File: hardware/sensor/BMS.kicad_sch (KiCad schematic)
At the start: 1 part, among them J4 Conn_01x04

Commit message: Fix incorrect upstream
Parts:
- removed J4: Conn_01x04, symbol Connector_Generic:Conn_01x04
- added J201: PWR, Connector_PinHeader_2.54mm:PinHeader_1x04_P2.54mm_Horizontal, symbol Connector:Conn_01x04_Pin
- added J202: control signals, Connector_PinHeader_2.54mm:PinHeader_1x06_P2.54mm_Horizontal, symbol Connector:Conn_01x06_Pin
- added J502: V_{DD}MCU, testpoint_519x:Testpoint_519xTR, symbol Connector:Conn_01x01_Pin
- added J502 (x3): GND, testpoint_519x:Testpoint_519xTR, symbol Connector:Conn_01x01_Pin
- added J502: V_{DD}AN, testpoint_519x:Testpoint_519xTR, symbol Connector:Conn_01x01_Pin
- added J502: LDO_{EN}, testpoint_519x:Testpoint_519xTR, symbol Connector:Conn_01x01_Pin
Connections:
- net GND: now also J201.2 (Pin_2), J201.3 (Pin_3), J202.5 (Pin_5), J502.1 (Pin_1), J502.1 (Pin_1), J502.1 (Pin_1)
- net V_{Out}: now also J201.4 (Pin_4), J502.1 (Pin_1)
- new net EH-ON: J202.3 (Pin_3)
- new net HBO-MCU: J202.4 (Pin_4)
- new net LDO_{EN}: J202.6 (Pin_6), J502.1 (Pin_1)
- new net LDO_{OUT}: J201.1 (Pin_1), J502.1 (Pin_1)
- new net PWG-LDO: J202.1 (Pin_1)
- new net PWG-Vout: J202.2 (Pin_2)

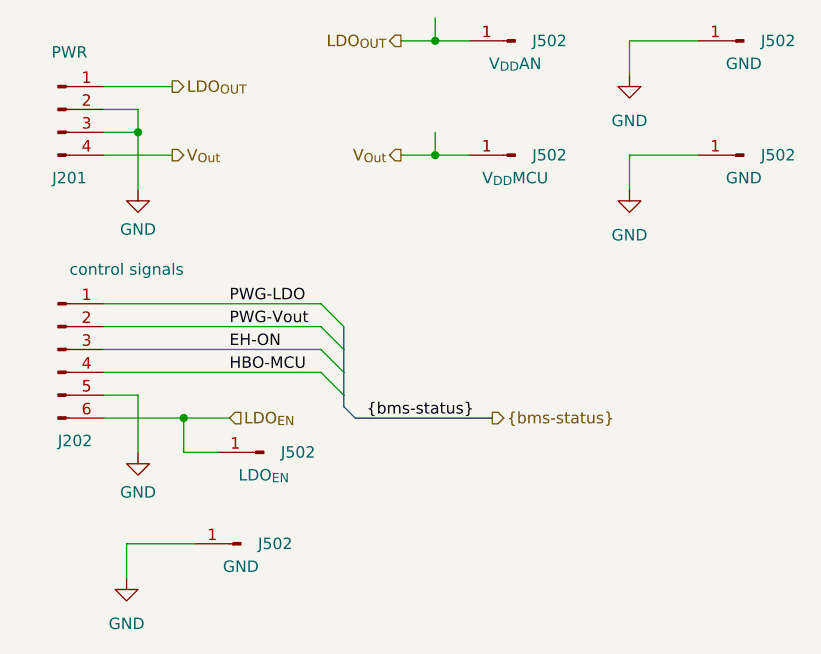
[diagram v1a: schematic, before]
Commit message: Finished initial pcb routing
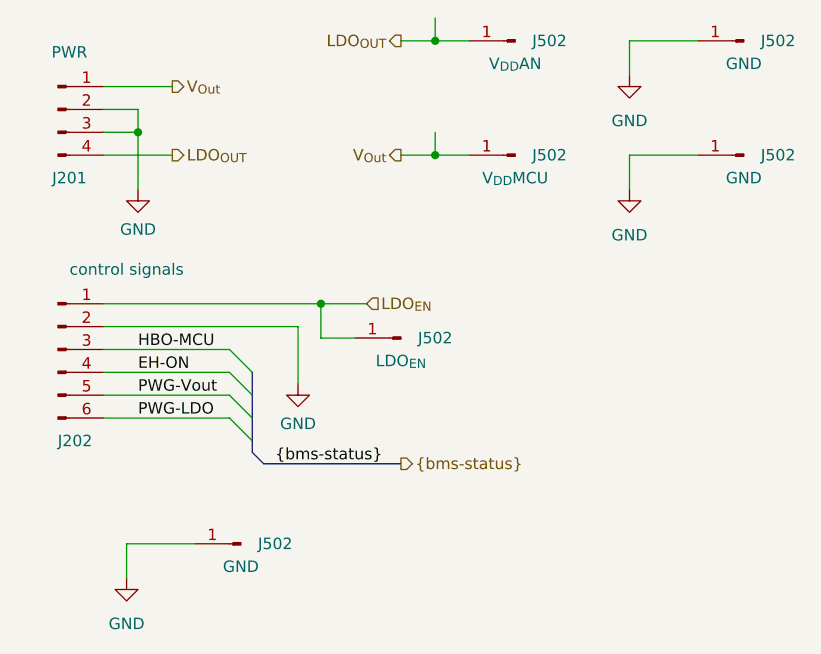
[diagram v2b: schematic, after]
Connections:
- net EH-ON: now also J202.4 (Pin_4); no longer J202.3 (Pin_3)
- net GND: now also J202.2 (Pin_2); no longer J202.5 (Pin_5)
- net HBO-MCU: now also J202.3 (Pin_3); no longer J202.4 (Pin_4)
- net LDO_{EN}: now also J202.1 (Pin_1); no longer J202.6 (Pin_6)
- net LDO_{OUT}: now also J201.4 (Pin_4); no longer J201.1 (Pin_1)
- net PWG-LDO: now also J202.6 (Pin_6); no longer J202.1 (Pin_1)
- net PWG-Vout: now also J202.5 (Pin_5); no longer J202.2 (Pin_2)
- net V_{Out}: now also J201.1 (Pin_1); no longer J201.4 (Pin_4)
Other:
- moved on the sheet: J502
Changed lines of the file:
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@@
   (junction (at 102.87 35.56) (diameter 0) (color 0 0 0 0)
   )
-  (junction (at 74.93 77.47) (diameter 0) (color 0 0 0 0)
-  )
   (junction (at 69.85 45.72) (diameter 0) (color 0 0 0 0)
   )
+  (junction (at 90.17 64.77) (diameter 0) (color 0 0 0 0)
+  )
   (junction (at 102.87 48.26) (diameter 0) (color 0 0 0 0)
   )
-  (bus_entry (at 90.17 69.85) (size 2.54 2.54)
-    (stroke (width 0) (type default))
-  )
-  (bus_entry (at 90.17 72.39) (size 2.54 2.54)
-    (stroke (width 0) (type default))
-  )
-  (bus_entry (at 90.17 64.77) (size 2.54 2.54)
-    (stroke (width 0) (type default))
-  )
-  (bus_entry (at 90.17 67.31) (size 2.54 2.54)
-    (stroke (width 0) (type default))
-  )
-  (wire (pts (xy 74.93 77.47) (xy 66.04 77.47))
-    (stroke (width 0) (type default))
-  )
-  (wire (pts (xy 69.85 74.93) (xy 69.85 81.28))
-    (stroke (width 0) (type default))
-  )
-  (bus (pts (xy 92.71 67.31) (xy 92.71 69.85))
+  (bus_entry (at 80.01 74.93) (size 2.54 2.54)
+    (stroke (width 0) (type default))
+  )
+  (bus_entry (at 80.01 77.47) (size 2.54 2.54)
+    (stroke (width 0) (type default))
+  )
+  (bus_entry (at 80.01 69.85) (size 2.54 2.54)
+    (stroke (width 0) (type default))
+  )
+  (bus_entry (at 80.01 72.39) (size 2.54 2.54)
+    (stroke (width 0) (type default))
+  )
+  (wire (pts (xy 66.04 77.47) (xy 80.01 77.47))
+    (stroke (width 0) (type default))
+  )
+  (wire (pts (xy 87.63 67.31) (xy 87.63 73.66))
+    (stroke (width 0) (type default))
+  )
+  (bus (pts (xy 82.55 72.39) (xy 82.55 74.93))
     (stroke (width 0) (type default))
   )
@@
     (stroke (width 0) (type default))
   )
-  (wire (pts (xy 66.04 69.85) (xy 90.17 69.85))
+  (wire (pts (xy 66.04 69.85) (xy 80.01 69.85))
     (stroke (width 0) (type default))
   )
@@
     (stroke (width 0) (type default))
   )
-  (wire (pts (xy 66.04 67.31) (xy 90.17 67.31))
-    (stroke (width 0) (type default))
-  )
-  (wire (pts (xy 74.93 81.28) (xy 74.93 77.47))
-    (stroke (width 0) (type default))
-  )
-  (wire (pts (xy 80.01 77.47) (xy 74.93 77.47))
-    (stroke (width 0) (type default))
-  )
-  (wire (pts (xy 66.04 72.39) (xy 90.17 72.39))
-    (stroke (width 0) (type default))
-  )
-  (wire (pts (xy 66.04 74.93) (xy 69.85 74.93))
-    (stroke (width 0) (type default))
-  )
-  (bus (pts (xy 93.98 77.47) (xy 109.22 77.47))
+  (wire (pts (xy 66.04 67.31) (xy 87.63 67.31))
+    (stroke (width 0) (type default))
+  )
+  (wire (pts (xy 90.17 68.58) (xy 90.17 64.77))
+    (stroke (width 0) (type default))
+  )
+  (wire (pts (xy 95.25 64.77) (xy 90.17 64.77))
+    (stroke (width 0) (type default))
+  )
+  (wire (pts (xy 66.04 72.39) (xy 80.01 72.39))
+    (stroke (width 0) (type default))
+  )
+  (bus (pts (xy 83.82 82.55) (xy 99.06 82.55))
     (stroke (width 0) (type default))
   )
@@
     (stroke (width 0) (type default))
   )
-  (bus (pts (xy 92.71 72.39) (xy 92.71 74.93))
-    (stroke (width 0) (type default))
-  )
-  (wire (pts (xy 78.74 81.28) (xy 74.93 81.28))
+  (bus (pts (xy 82.55 77.47) (xy 82.55 80.01))
+    (stroke (width 0) (type default))
+  )
+  (wire (pts (xy 93.98 68.58) (xy 90.17 68.58))
     (stroke (width 0) (type default))
   )
@@
     (stroke (width 0) (type default))
   )
-  (bus (pts (xy 92.71 74.93) (xy 92.71 76.2))
-    (stroke (width 0) (type default))
-  )
-  (bus (pts (xy 92.71 76.2) (xy 93.98 77.47))
+  (bus (pts (xy 82.55 80.01) (xy 82.55 81.28))
+    (stroke (width 0) (type default))
+  )
+  (bus (pts (xy 82.55 81.28) (xy 83.82 82.55))
     (stroke (width 0) (type default))
   )
@@
     (stroke (width 0) (type default))
   )
-  (bus (pts (xy 92.71 69.85) (xy 92.71 72.39))
+  (bus (pts (xy 82.55 74.93) (xy 82.55 77.47))
     (stroke (width 0) (type default))
   )
@@
     (stroke (width 0) (type default))
   )
+  (wire (pts (xy 66.04 74.93) (xy 80.01 74.93))
+    (stroke (width 0) (type default))
+  )
   (wire (pts (xy 66.04 64.77) (xy 90.17 64.77))
     (stroke (width 0) (type default))
@@
     (stroke (width 0) (type default))
   )
-  (label "PWG-Vout" (at 80.01 67.31 0) (fields_autoplaced)
-    (effects (font (size 1.27 1.27)) (justify left bottom))
-  )
-  (label "{bms-status}" (at 95.25 77.47 0) (fields_autoplaced)
-    (effects (font (size 1.27 1.27)) (justify left bottom))
-  )
-  (label "PWG-LDO" (at 80.01 64.77 0) (fields_autoplaced)
-    (effects (font (size 1.27 1.27)) (justify left bottom))
-  )
-  (label "HBO-MCU" (at 80.01 72.39 0) (fields_autoplaced)
-    (effects (font (size 1.27 1.27)) (justify left bottom))
-  )
-  (label "EH-ON" (at 80.01 69.85 0) (fields_autoplaced)
-    (effects (font (size 1.27 1.27)) (justify left bottom))
-  )
-  (hierarchical_label "LDO_{OUT}" (shape output) (at 73.66 40.64 0) (fields_autoplaced)
+  (label "PWG-Vout" (at 69.85 74.93 0) (fields_autoplaced)
+    (effects (font (size 1.27 1.27)) (justify left bottom))
+  )
+  (label "{bms-status}" (at 85.09 82.55 0) (fields_autoplaced)
+    (effects (font (size 1.27 1.27)) (justify left bottom))
+  )
+  (label "PWG-LDO" (at 69.85 77.47 0) (fields_autoplaced)
+    (effects (font (size 1.27 1.27)) (justify left bottom))
+  )
+  (label "HBO-MCU" (at 69.85 69.85 0) (fields_autoplaced)
+    (effects (font (size 1.27 1.27)) (justify left bottom))
+  )
+  (label "EH-ON" (at 69.85 72.39 0) (fields_autoplaced)
+    (effects (font (size 1.27 1.27)) (justify left bottom))
+  )
+  (hierarchical_label "LDO_{OUT}" (shape output) (at 73.66 48.26 0) (fields_autoplaced)
     (effects (font (size 1.27 1.27)) (justify left))
   )
@@
     (effects (font (size 1.27 1.27)) (justify right))
   )
-  (hierarchical_label "{bms-status}" (shape output) (at 109.22 77.47 0) (fields_autoplaced)
+  (hierarchical_label "{bms-status}" (shape output) (at 99.06 82.55 0) (fields_autoplaced)
     (effects (font (size 1.27 1.27)) (justify left))
   )
-  (hierarchical_label "V_{Out}" (shape output) (at 73.66 48.26 0) (fields_autoplaced)
+  (hierarchical_label "V_{Out}" (shape output) (at 73.66 40.64 0) (fields_autoplaced)
     (effects (font (size 1.27 1.27)) (justify left))
   )
@@
     (effects (font (size 1.27 1.27)) (justify right))
   )
-  (hierarchical_label "LDO_{EN}" (shape input) (at 80.01 77.47 0) (fields_autoplaced)
+  (hierarchical_label "LDO_{EN}" (shape input) (at 95.25 64.77 0) (fields_autoplaced)
     (effects (font (size 1.27 1.27)) (justify left))
   )
@@
     )
   )
-  (symbol (lib_id "Connector:Conn_01x01_Pin") (at 83.82 81.28 180) (unit 1)
-    (in_bom yes) (on_board yes) (dnp no)
-    (property "Reference" "J502" (at 87.63 81.28 0)
-      (effects (font (size 1.27 1.27)))
-    )
-    (property "Value" "LDO_{EN}" (at 83.82 83.82 0)
-      (effects (font (size 1.27 1.27)))
-    )
-    (property "Footprint" "testpoint_519x:Testpoint_519xTR" (at 83.82 81.28 0)
-      (effects (font (size 1.27 1.27)) hide)
-    )
-    (property "Datasheet" "~" (at 83.82 81.28 0)
+  (symbol (lib_id "Connector:Conn_01x01_Pin") (at 99.06 68.58 180) (unit 1)
+    (in_bom yes) (on_board yes) (dnp no)
+    (property "Reference" "J502" (at 102.87 68.58 0)
+      (effects (font (size 1.27 1.27)))
+    )
+    (property "Value" "LDO_{EN}" (at 99.06 71.12 0)
+      (effects (font (size 1.27 1.27)))
+    )
+    (property "Footprint" "testpoint_519x:Testpoint_519xTR" (at 99.06 68.58 0)
+      (effects (font (size 1.27 1.27)) hide)
+    )
+    (property "Datasheet" "~" (at 99.06 68.58 0)
       (effects (font (size 1.27 1.27)) hide)
     )
@@
     )
   )
-  (symbol (lib_id "power:GND") (at 69.85 81.28 0) (unit 1)
+  (symbol (lib_id "power:GND") (at 87.63 73.66 0) (unit 1)
     (in_bom yes) (on_board yes) (dnp no) (fields_autoplaced)
-    (property "Reference" "#PWR0203" (at 69.85 87.63 0)
-      (effects (font (size 1.27 1.27)) hide)
-    )
-    (property "Value" "GND" (at 69.85 85.725 0)
-      (effects (font (size 1.27 1.27)))
-    )
-    (property "Footprint" "" (at 69.85 81.28 0)
-      (effects (font (size 1.27 1.27)) hide)
-    )
-    (property "Datasheet" "" (at 69.85 81.28 0)
-      (effects (font (size 1.27 1.27)) hide)
-    )
+    (property "Reference" "#PWR0203" (at 87.63 80.01 0)
+      (effects (font (size 1.27 1.27)) hide)
+    )
+    (property "Value" "GND" (at 87.63 78.105 0)
+      (effects (font (size 1.27 1.27)))
+    )
+    (property "Footprint" "" (at 87.63 73.66 0)
+      (effects (font (size 1.27 1.27)) hide)
+    )
+    (property "Datasheet" "" (at 87.63 73.66 0)
+      (effects (font (size 1.27 1.27)) hide)
+    )
